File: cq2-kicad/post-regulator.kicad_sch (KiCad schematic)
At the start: 75 parts, among them Q3 XPH4R10, U19 AD8479, U31 TLV9151, U32 TLV9151, U33 TLV9151, U34 TLV9151, U35 TLV9151, U36 TLV9151, U37 TLV9151

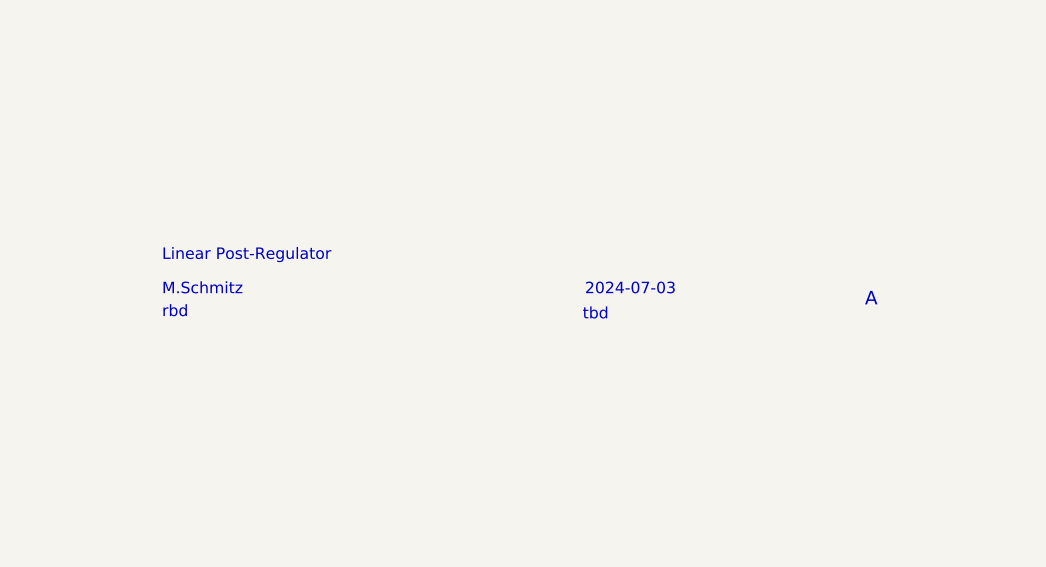
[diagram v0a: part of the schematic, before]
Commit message: drc checked before panalization
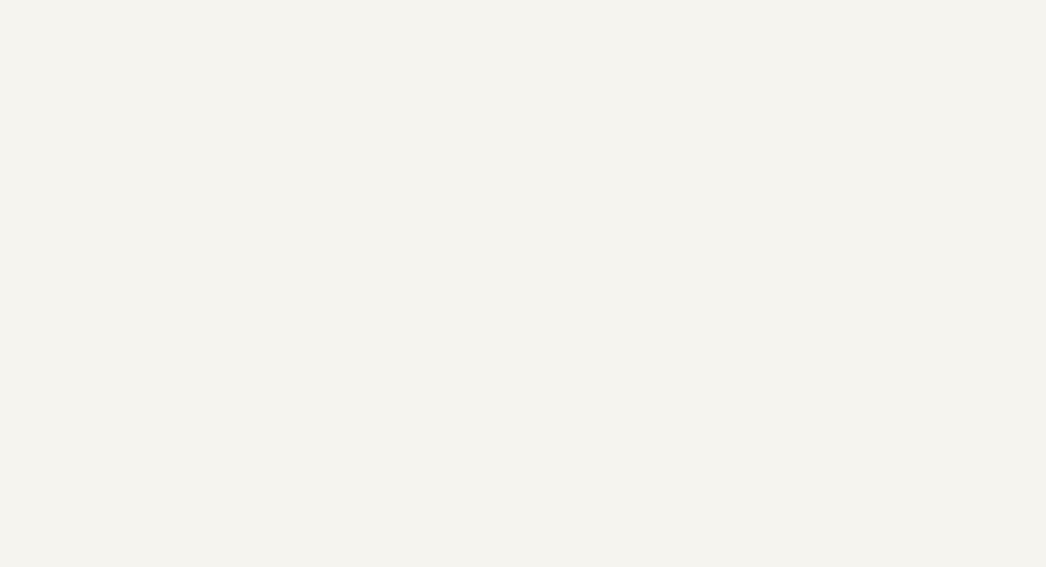
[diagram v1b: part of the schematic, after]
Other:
- note removed: "2024-07-03"
- note removed: "Linear Post-Regulator"
- note removed: "M.Schmitz"
- note removed: "rbd"
- note removed: "tbd"
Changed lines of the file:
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@@
 	(title_block
 		(title "CQ2")
-		(date "2024-07-17")
+		(date "2024-07-31")
 		(rev "0")
+		(comment 1 "Linear Post-Regulator")
+		(comment 2 "Manfred Schmitz")
+		(comment 3 "tbd")
+		(comment 4 "2024-07-03")
+		(comment 5 "tbd")
+		(comment 6 "A")
 	)
 	(junction
@@
 		)
 	)
-	(text "Linear Post-Regulator"
-		(exclude_from_sim no)
-		(at 190.754 187.198 0)
-		(effects
-			(font
-				(size 1.27 1.27)
-			)
-			(justify left bottom)
-		)
-	)
-	(text "A"
-		(exclude_from_sim no)
-		(at 268.859 192.278 0)
-		(effects
-			(font
-				(size 1.4986 1.4986)
-			)
-			(justify left bottom)
-		)
-	)
 	(text "FSR = ±6.144"
 		(exclude_from_sim no)
@@
 		)
 	)
-	(text "M.Schmitz"
-		(exclude_from_sim no)
-		(at 190.754 191.008 0)
-		(effects
-			(font
-				(size 1.27 1.27)
-			)
-			(justify left bottom)
-		)
-	)
 	(text "Fullscale 2A -> 2V"
 		(exclude_from_sim no)
@@
 		)
 	)
-	(text "rbd"
-		(exclude_from_sim no)
-		(at 190.754 193.548 0)
-		(effects
-			(font
-				(size 1.27 1.27)
-			)
-			(justify left bottom)
-		)
-	)
 	(text "-2 V"
 		(exclude_from_sim no)
@@
 		)
 	)
-	(text "2024-07-03"
-		(exclude_from_sim no)
-		(at 237.744 191.008 0)
-		(effects
-			(font
-				(size 1.27 1.27)
-			)
-			(justify left bottom)
-		)
-	)
-	(text "tbd"
-		(exclude_from_sim no)
-		(at 237.49 193.802 0)
-		(effects
-			(font
-				(size 1.27 1.27)
-			)
-			(justify left bottom)
-		)
-	)

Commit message: Production documents created
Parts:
- Q3: Outline (none) -> SMT SOP-Advance-8
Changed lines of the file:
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@@
 	(title_block
 		(title "CQ2")
-		(date "2024-07-31")
+		(date "2024-08-03")
 		(rev "0")
 		(comment 1 "Linear Post-Regulator")
@@
 			)
 		)
-		(property "Description" "Transistor MOSFET N-Channel - SMT"
+		(property "Description" "Transistor MOSFET N-Channel"
 			(at 152.4 92.71 0)
 			(effects
@@
 			)
 		)
-		(property "Outline" ""
+		(property "Outline" "SMT SOP-Advance-8"
 			(at 152.4 92.71 0)
 			(effects

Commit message: cq2 adapter in work
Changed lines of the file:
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@@
 (kicad_sch
-	(version 20231120)
+	(version 20250114)
 	(generator "eeschema")
-	(generator_version "8.0")
+	(generator_version "9.0")
 	(paper "A4")
 	(title_block
@@
 		(comment 6 "A")
 	)
+	(text "FSR = ±2.048V"
+		(exclude_from_sim no)
+		(at 51.054 152.4 0)
+		(effects
+			(font
+				(size 1.27 1.27)
+				(color 0 0 194 1)
+			)
+			(justify left bottom)
+		)
+	)
+	(text "A"
+		(exclude_from_sim no)
+		(at 287.147 231.14 0)
+		(effects
+			(font
+				(size 1.4986 1.4986)
+			)
+			(justify left bottom)
+		)
+	)
+	(text "FSR = ±6.144"
+		(exclude_from_sim no)
+		(at 201.93 134.62 0)
+		(effects
+			(font
+				(size 1.27 1.27)
+				(color 0 0 194 1)
+			)
+			(justify left bottom)
+		)
+	)
+	(text "50V ->\n4.219V"
+		(exclude_from_sim no)
+		(at 264.414 139.7 0)
+		(effects
+			(font
+				(size 1.27 1.27)
+			)
+		)
+	)
+	(text "50V ->\n2.381V"
+		(exclude_from_sim no)
+		(at 251.714 66.802 0)
+		(effects
+			(font
+				(size 1.27 1.27)
+			)
+		)
+	)
+	(text "Fullscale 2A -> 2V"
+		(exclude_from_sim no)
+		(at 51.054 154.94 0)
+		(effects
+			(font
+				(size 1.27 1.27)
+				(color 0 0 194 1)
+			)
+			(justify left bottom)
+		)
+	)
+	(text "22 MOhm Impendanz"
+		(exclude_from_sim no)
+		(at 201.93 132.08 0)
+		(effects
+			(font
+				(size 1.27 1.27)
+				(color 0 0 194 1)
+			)
+			(justify left bottom)
+		)
+	)
+	(text "-2 V"
+		(exclude_from_sim no)
+		(at 77.47 72.39 0)
+		(effects
+			(font
+				(size 1.27 1.27)
+			)
+		)
+	)
+	(text "Fullscale 50V -> 4.2962V"
+		(exclude_from_sim no)
+		(at 201.93 137.16 0)
+		(effects
+			(font
+				(size 1.27 1.27)
+				(color 0 0 194 1)
+			)
+			(justify left bottom)
+		)
+	)
 	(junction
 		(at 233.68 139.7)
@@
 		)
 	)
-	(text "FSR = ±2.048V"
-		(exclude_from_sim no)
-		(at 51.054 152.4 0)
-		(effects
-			(font
-				(size 1.27 1.27)
-				(color 0 0 194 1)
-			)
-			(justify left bottom)
-		)
-	)
-	(text "A"
-		(exclude_from_sim no)
-		(at 287.147 231.14 0)
-		(effects
-			(font
-				(size 1.4986 1.4986)
-			)
-			(justify left bottom)
-		)
-	)
-	(text "FSR = ±6.144"
-		(exclude_from_sim no)
-		(at 201.93 134.62 0)
-		(effects
-			(font
-				(size 1.27 1.27)
-				(color 0 0 194 1)
-			)
-			(justify left bottom)
-		)
-	)
-	(text "50V ->\n4.219V"
-		(exclude_from_sim no)
-		(at 264.414 139.7 0)
-		(effects
-			(font
-				(size 1.27 1.27)
-			)
-		)
-	)
-	(text "50V ->\n2.381V"
-		(exclude_from_sim no)
-		(at 251.714 66.802 0)
-		(effects
-			(font
-				(size 1.27 1.27)
-			)
-		)
-	)
-	(text "Fullscale 2A -> 2V"
-		(exclude_from_sim no)
-		(at 51.054 154.94 0)
-		(effects
-			(font
-				(size 1.27 1.27)
-				(color 0 0 194 1)
-			)
-			(justify left bottom)
-		)
-	)
-	(text "22 MOhm Impendanz"
-		(exclude_from_sim no)
-		(at 201.93 132.08 0)
-		(effects
-			(font
-				(size 1.27 1.27)
-				(color 0 0 194 1)
-			)
-			(justify left bottom)
-		)
-	)
-	(text "-2 V"
-		(exclude_from_sim no)
-		(at 77.47 72.39 0)
-		(effects
-			(font
-				(size 1.27 1.27)
-			)
-		)
-	)
-	(text "Fullscale 50V -> 4.2962V"
-		(exclude_from_sim no)
-		(at 201.93 137.16 0)
-		(effects
-			(font
-				(size 1.27 1.27)
-				(color 0 0 194 1)
-			)
-			(justify left bottom)
-		)
-	)
 	(label "GND_ISO"
 		(at 215.9 40.64 0)
-		(fields_autoplaced yes)
 		(effects
 			(font
@@
 	(label "GND_ISO"
 		(at 74.93 143.51 180)
-		(fields_autoplaced yes)
 		(effects
 			(font
@@
 	(label "GND_ISO"
 		(at 83.82 57.15 180)
-		(fields_autoplaced yes)
 		(effects
 			(font
@@
 	(label "GND_ISO"
 		(at 215.9 25.4 0)
-		(fields_autoplaced yes)
 		(effects
 			(font
@@
 	(label "+5V_ISO"
 		(at 120.65 116.84 180)
-		(fields_autoplaced yes)
 		(effects
 			(font
@@
 	(label "GND_ISO"
 		(at 93.98 107.95 0)
-		(fields_autoplaced yes)
 		(effects
 			(font
@@
 	(label "GND_ISO"
 		(at 120.65 129.54 180)
-		(fields_autoplaced yes)
 		(effects
 			(font
@@
 	(label "+5V_ISO"
 		(at 48.26 92.71 180)
-		(fields_autoplaced yes)
 		(effects
 			(font
@@
 	(label "-5V_ISO"
 		(at 83.82 87.63 180)
-		(fields_autoplaced yes)
 		(effects
 			(font
@@
 	(label "GND_ISO"
 		(at 215.9 152.4 0)
-		(fields_autoplaced yes)
 		(effects
 			(font
@@
 		(shape input)
 		(at 27.94 50.8 180)
-		(fields_autoplaced yes)
 		(effects
 			(font
@@
 		(shape input)
 		(at 48.26 132.08 180)
-		(fields_autoplaced yes)
 		(effects
 			(font
@@
 		(shape input)
 		(at 24.13 33.02 180)
-		(fields_autoplaced yes)
 		(effects
 			(font
@@
 		(shape input)
 		(at 271.78 27.94 0)
-		(fields_autoplaced yes)
 		(effects
 			(font
@@
 		(shape input)
 		(at 24.13 22.86 180)
-		(fields_autoplaced yes)
 		(effects
 			(font
@@
 		(shape output)
 		(at 271.78 87.63 0)
-		(fields_autoplaced yes)
 		(effects
 			(font
@@
 		(shape input)
 		(at 27.94 113.03 180)
-		(fields_autoplaced yes)
 		(effects
 			(font
@@
 		(shape output)
 		(at 27.94 74.93 180)
-		(fields_autoplaced yes)
 		(effects
 			(font
@@
 		(shape output)
 		(at 271.78 50.8 0)
-		(fields_autoplaced yes)
 		(effects
 			(font
@@
 		(shape input)
 		(at 27.94 95.25 180)
-		(fields_autoplaced yes)
 		(effects
 			(font
@@
 		(shape input)
 		(at 271.78 113.03 0)
-		(fields_autoplaced yes)
 		(effects
 			(font
@@
 		(shape input)
 		(at 215.9 120.65 180)
-		(fields_autoplaced yes)
 		(effects
 			(font
@@
 		(shape input)
 		(at 49.53 156.21 180)
-		(fields_autoplaced yes)
 		(effects
 			(font
@@
 		(shape input)
 		(at 215.9 139.7 180)
-		(fields_autoplaced yes)
 		(effects
 			(font
@@
 		(shape input)
 		(at 24.13 43.18 180)
-		(fields_autoplaced yes)
 		(effects
 			(font
@@
 		(shape output)
 		(at 27.94 92.71 180)
-		(fields_autoplaced yes)
 		(effects
 			(font
@@
 		(shape input)
 		(at 49.53 148.59 180)
-		(fields_autoplaced yes)
 		(effects
 			(font
@@
 		(shape input)
 		(at 49.53 170.18 180)
-		(fields_autoplaced yes)
 		(effects
 			(font
